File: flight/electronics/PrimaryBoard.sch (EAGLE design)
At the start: 10 parts

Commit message: primary board updates
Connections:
- net +5V: no longer ESP32.VIN
- net VBAT: now also ESP32.VIN
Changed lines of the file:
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@@
 <part name="ARDUCAM-B" library="Rembrandt Electronics - JST XH Connectors v1-0" deviceset="JST-XH-06-PIN" device=""/>
 <part name="GND8" library="supply1" library_urn="urn:adsk.eagle:library:371" deviceset="GND" device=""/>
-<part name="P+3" library="supply1" library_urn="urn:adsk.eagle:library:371" deviceset="+5V" device=""/>
 <part name="+3V4" library="supply1" library_urn="urn:adsk.eagle:library:371" deviceset="+3V3" device=""/>
 <part name="SENSOR_BOARD" library="Rembrandt Electronics - JST XH Connectors v1-0" deviceset="JST-XH-10-PIN" device=""/>
@@
 <attribute name="VALUE" x="22.86" y="-7.62" size="1.778" layer="96"/>
 </instance>
-<instance part="P+3" gate="1" x="50.8" y="88.9" smashed="yes">
-<attribute name="VALUE" x="48.26" y="83.82" size="1.778" layer="96" rot="R90"/>
-</instance>
 <instance part="+3V4" gate="G$1" x="22.86" y="17.78" smashed="yes">
 <attribute name="VALUE" x="20.32" y="12.7" size="1.778" layer="96" rot="R90"/>
@@
 <wire x1="114.3" y1="40.64" x2="116.84" y2="40.64" width="0.1524" layer="91"/>
 </segment>
-<segment>
-<pinref part="P+3" gate="1" pin="+5V"/>
-<wire x1="50.8" y1="86.36" x2="50.8" y2="83.82" width="0.1524" layer="91"/>
-<pinref part="ESP32" gate="G$1" pin="VIN"/>
-<wire x1="50.8" y1="83.82" x2="53.34" y2="83.82" width="0.1524" layer="91"/>
-</segment>
 </net>
 <net name="GND" class="0">
@@
 <wire x1="99.06" y1="111.76" x2="99.06" y2="71.12" width="0.1524" layer="91"/>
 <wire x1="99.06" y1="71.12" x2="106.68" y2="71.12" width="0.1524" layer="91"/>
+<pinref part="ESP32" gate="G$1" pin="VIN"/>
+<wire x1="50.8" y1="83.82" x2="53.34" y2="83.82" width="0.1524" layer="91"/>
+<wire x1="50.8" y1="83.82" x2="50.8" y2="111.76" width="0.1524" layer="91"/>
+<wire x1="50.8" y1="111.76" x2="99.06" y2="111.76" width="0.1524" layer="91"/>
+<junction x="99.06" y="111.76"/>
 </segment>
 </net>

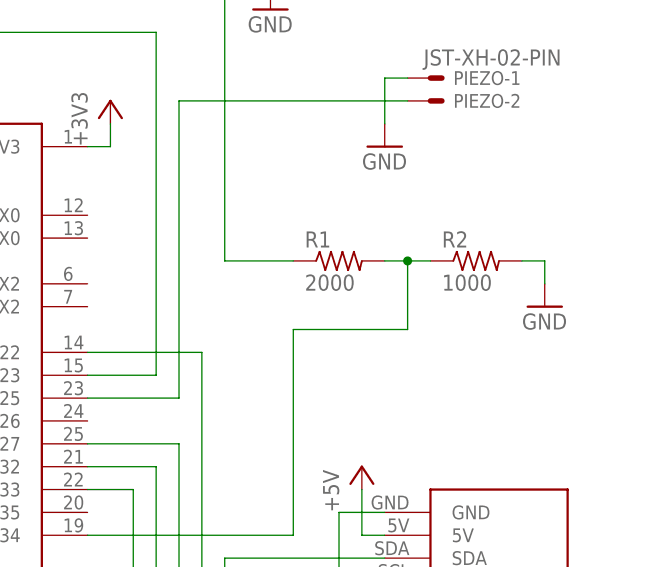
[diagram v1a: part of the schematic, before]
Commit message: shrink primary to 90mm
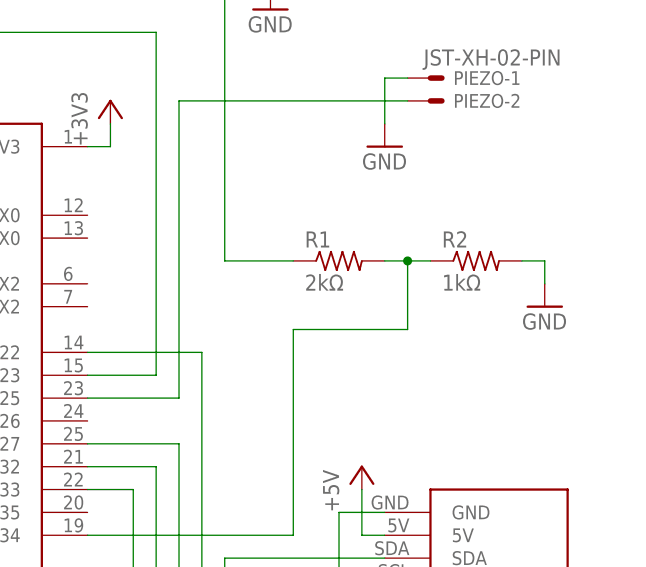
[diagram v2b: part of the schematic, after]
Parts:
- R1: value 2000 -> 2kΩ
- R2: value 1000 -> 1kΩ
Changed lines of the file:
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@@
 <part name="P+2" library="supply1" library_urn="urn:adsk.eagle:library:371" deviceset="+5V" device=""/>
 <part name="GND5" library="supply1" library_urn="urn:adsk.eagle:library:371" deviceset="GND" device=""/>
-<part name="R1" library="rcl" library_urn="urn:adsk.eagle:library:334" deviceset="R-US_" device="0207/10" package3d_urn="urn:adsk.eagle:package:23491/2" value="2000"/>
-<part name="R2" library="rcl" library_urn="urn:adsk.eagle:library:334" deviceset="R-US_" device="0207/10" package3d_urn="urn:adsk.eagle:package:23491/2" value="1000"/>
+<part name="R1" library="rcl" library_urn="urn:adsk.eagle:library:334" deviceset="R-US_" device="0207/10" package3d_urn="urn:adsk.eagle:package:23491/2" value="2kΩ"/>
+<part name="R2" library="rcl" library_urn="urn:adsk.eagle:library:334" deviceset="R-US_" device="0207/10" package3d_urn="urn:adsk.eagle:package:23491/2" value="1kΩ"/>
 <part name="GND6" library="supply1" library_urn="urn:adsk.eagle:library:371" deviceset="GND" device=""/>
 <part name="PIEZO" library="Rembrandt Electronics - JST XH Connectors v1-0" deviceset="JST-XH-02-PIN" device=""/>

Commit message: primary board redesign
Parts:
- removed SENSOR_BOARD: JST-XH-10-PIN, Rembrandt Electronics - JST XH Connectors v1-0:JST-XH-10-PIN
- added H1, H2, H3, H4: MOUNT-PAD-ROUND3.0, holes:MOUNT-PAD-ROUND3.0
- added X1: JST-XH-07-PIN, Rembrandt Electronics - JST XH Connectors v1-0:JST-XH-07-PIN
- U$2: value DS1307BREAKOUT -> PCF8523BREAKOUT; device Breakouts:DS1307BREAKOUT -> Breakouts:PCF8523BREAKOUT
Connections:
- removed net +5V: POWER_BOARD-3.S, U$2.5V
- removed net MOSI_CLK: ESP32.D14, SENSOR_BOARD-8.S, U$1.CLK
- new net HSPI_CLK: ESP32.D14, U$1.CLK
- net +3V3: now also POWER_BOARD-2.S, U$2.VCC, X1-2.S; no longer SENSOR_BOARD-10.S
- net GND: now also H1.MOUNT, H2.MOUNT, H3.MOUNT, H4.MOUNT, POWER_BOARD-1.S, X1-1.S; no longer POWER_BOARD-2.S, SENSOR_BOARD-9.S
- net GPIO1: now also X1-5.S; no longer SENSOR_BOARD-1.S
- net GPIO2: now also X1-6.S; no longer SENSOR_BOARD-2.S
- net GPIO3: now also X1-7.S; no longer SENSOR_BOARD-3.S
- net HSPI_MISO: no longer SENSOR_BOARD-7.S
- net HSPI_MOSI: no longer SENSOR_BOARD-6.S
- net I2C_SCL: now also X1-3.S; no longer SENSOR_BOARD-5.S
- net I2C_SDA: now also X1-4.S; no longer SENSOR_BOARD-4.S
- net SD_CS: now also ESP32.D15; no longer ESP32.D2
- net VBAT: now also POWER_BOARD-3.S; no longer ESP32.VIN, POWER_BOARD-1.S
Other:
- moved on the sheet: ARDUCAM-A-1, ARDUCAM-A-2, ARDUCAM-A-3, ARDUCAM-A-4, ARDUCAM-A-5, ARDUCAM-A-6, ARDUCAM-B-1, ARDUCAM-B-2, ARDUCAM-B-3, ARDUCAM-B-4, ARDUCAM-B-5, ARDUCAM-B-6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

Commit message: final board tweaks
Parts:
- removed POWER_BOARD: JST-XH-03-PIN, Rembrandt Electronics - JST XH Connectors v1-0:JST-XH-03-PIN
- added X2: JST-XH-03-PIN, JST-XH Connectors:JST-XH-03-PIN
- ARDUCAM-A, ARDUCAM-B: device Rembrandt Electronics - JST XH Connectors v1-0:JST-XH-06-PIN -> JST-XH Connectors:JST-XH-06-PIN
- PIEZO: device Rembrandt Electronics - JST XH Connectors v1-0:JST-XH-02-PIN -> JST-XH Connectors:JST-XH-02-PIN
- X1: device Rembrandt Electronics - JST XH Connectors v1-0:JST-XH-07-PIN -> JST-XH Connectors:JST-XH-07-PIN
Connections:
- net +3V3: now also X2-2.S; no longer POWER_BOARD-2.S
- net GND: now also X2-1.S; no longer POWER_BOARD-1.S
- net VBAT: now also X2-3.S; no longer POWER_BOARD-3.S
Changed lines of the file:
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@@
 <part name="GND1" library="supply1" library_urn="urn:adsk.eagle:library:371" deviceset="GND" device=""/>
 <part name="GND2" library="supply1" library_urn="urn:adsk.eagle:library:371" deviceset="GND" device=""/>
-<part name="ARDUCAM-A" library="Rembrandt Electronics - JST XH Connectors v1-0" deviceset="JST-XH-06-PIN" device="" value="JST-XH-06-PIN"/>
+<part name="ARDUCAM-A" library="JST-XH Connectors" deviceset="JST-XH-06-PIN" device="" value="JST-XH-06-PIN"/>
 <part name="GND3" library="supply1" library_urn="urn:adsk.eagle:library:371" deviceset="GND" device=""/>
 <part name="+3V3" library="supply1" library_urn="urn:adsk.eagle:library:371" deviceset="+3V3" device=""/>
 <part name="GND4" library="supply1" library_urn="urn:adsk.eagle:library:371" deviceset="GND" device=""/>
 <part name="U$1" library="Breakouts" deviceset="MICROSDBREAKOUT5V" device=""/>
-<part name="POWER_BOARD" library="Rembrandt Electronics - JST XH Connectors v1-0" deviceset="JST-XH-03-PIN" device=""/>
 <part name="GND5" library="supply1" library_urn="urn:adsk.eagle:library:371" deviceset="GND" device=""/>
 <part name="R1" library="rcl" library_urn="urn:adsk.eagle:library:334" deviceset="R-US_" device="0207/10" package3d_urn="urn:adsk.eagle:package:23491/2" value="2kΩ"/>
 <part name="R2" library="rcl" library_urn="urn:adsk.eagle:library:334" deviceset="R-US_" device="0207/10" package3d_urn="urn:adsk.eagle:package:23491/2" value="1kΩ"/>
 <part name="GND6" library="supply1" library_urn="urn:adsk.eagle:library:371" deviceset="GND" device=""/>
-<part name="PIEZO" library="Rembrandt Electronics - JST XH Connectors v1-0" deviceset="JST-XH-02-PIN" device=""/>
+<part name="PIEZO" library="JST-XH Connectors" deviceset="JST-XH-02-PIN" device=""/>
 <part name="GND7" library="supply1" library_urn="urn:adsk.eagle:library:371" deviceset="GND" device=""/>
-<part name="ARDUCAM-B" library="Rembrandt Electronics - JST XH Connectors v1-0" deviceset="JST-XH-06-PIN" device=""/>
+<part name="ARDUCAM-B" library="JST-XH Connectors" deviceset="JST-XH-06-PIN" device=""/>
 <part name="GND8" library="supply1" library_urn="urn:adsk.eagle:library:371" deviceset="GND" device=""/>
 <part name="+3V4" library="supply1" library_urn="urn:adsk.eagle:library:371" deviceset="+3V3" device=""/>
 <part name="+3V5" library="supply1" library_urn="urn:adsk.eagle:library:371" deviceset="+3V3" device=""/>
 <part name="GND9" library="supply1" library_urn="urn:adsk.eagle:library:371" deviceset="GND" device=""/>
-<part name="X1" library="Rembrandt Electronics - JST XH Connectors v1-0" deviceset="JST-XH-07-PIN" device=""/>
+<part name="X1" library="JST-XH Connectors" deviceset="JST-XH-07-PIN" device=""/>
 <part name="+3V6" library="supply1" library_urn="urn:adsk.eagle:library:371" deviceset="+3V3" device=""/>
 <part name="U$2" library="Breakouts" deviceset="PCF8523BREAKOUT" device=""/>
@@
 <part name="H4" library="holes" library_urn="urn:adsk.eagle:library:237" deviceset="MOUNT-PAD-ROUND" device="3.0" package3d_urn="urn:adsk.eagle:package:14280/1"/>
 <part name="GND10" library="supply1" library_urn="urn:adsk.eagle:library:371" deviceset="GND" device=""/>
+<part name="X2" library="JST-XH Connectors" deviceset="JST-XH-03-PIN" device=""/>
 </parts>
 <sheets>
@@
 </instance>
 <instance part="U$1" gate="G$1" x="-27.94" y="60.96" smashed="yes" rot="MR0"/>
-<instance part="POWER_BOARD" gate="-1" x="109.22" y="111.76" smashed="yes">
-<attribute name="NAME" x="111.76" y="110.998" size="1.524" layer="95"/>
-<attribute name="VALUE" x="108.458" y="113.157" size="1.778" layer="96"/>
-</instance>
-<instance part="POWER_BOARD" gate="-2" x="109.22" y="109.22" smashed="yes">
-<attribute name="NAME" x="111.76" y="108.458" size="1.524" layer="95"/>
-</instance>
-<instance part="POWER_BOARD" gate="-3" x="109.22" y="106.68" smashed="yes">
-<attribute name="NAME" x="111.76" y="105.918" size="1.524" layer="95"/>
-</instance>
 <instance part="GND5" gate="1" x="111.76" y="27.94" smashed="yes">
 <attribute name="VALUE" x="109.22" y="25.4" size="1.778" layer="96"/>
@@
 <instance part="GND10" gate="1" x="53.34" y="-55.88" smashed="yes">
 <attribute name="VALUE" x="50.8" y="-58.42" size="1.778" layer="96"/>
+</instance>
+<instance part="X2" gate="-1" x="109.22" y="111.76" smashed="yes">
+<attribute name="NAME" x="111.76" y="110.998" size="1.524" layer="95"/>
+<attribute name="VALUE" x="108.458" y="113.157" size="1.778" layer="96"/>
+</instance>
+<instance part="X2" gate="-2" x="109.22" y="109.22" smashed="yes">
+<attribute name="NAME" x="111.76" y="108.458" size="1.524" layer="95"/>
+</instance>
+<instance part="X2" gate="-3" x="109.22" y="106.68" smashed="yes">
+<attribute name="NAME" x="111.76" y="105.918" size="1.524" layer="95"/>
 </instance>
 </instances>
@@
 <segment>
 <pinref part="GND4" gate="1" pin="GND"/>
-<wire x1="104.14" y1="109.22" x2="104.14" y2="104.14" width="0.1524" layer="91"/>
-<pinref part="POWER_BOARD" gate="-1" pin="S"/>
-<wire x1="104.14" y1="104.14" x2="104.14" y2="101.6" width="0.1524" layer="91"/>
+<wire x1="104.14" y1="111.76" x2="104.14" y2="101.6" width="0.1524" layer="91"/>
+<pinref part="X2" gate="-1" pin="S"/>
 <wire x1="106.68" y1="111.76" x2="104.14" y2="111.76" width="0.1524" layer="91"/>
-<wire x1="104.14" y1="111.76" x2="104.14" y2="109.22" width="0.1524" layer="91"/>
 </segment>
 <segment>
@@
 <segment>
 <pinref part="+3V6" gate="G$1" pin="+3V3"/>
-<pinref part="POWER_BOARD" gate="-2" pin="S"/>
 <wire x1="101.6" y1="109.22" x2="101.6" y2="116.84" width="0.1524" layer="91"/>
-<wire x1="106.68" y1="109.22" x2="101.6" y2="109.22" width="0.1524" layer="91"/>
+<pinref part="X2" gate="-2" pin="S"/>
+<wire x1="101.6" y1="109.22" x2="106.68" y2="109.22" width="0.1524" layer="91"/>
 </segment>
 <segment>
@@
 <net name="VBAT" class="0">
 <segment>
-<label x="99.06" y="106.68" size="1.778" layer="95" rot="MR0" xref="yes"/>
-<pinref part="POWER_BOARD" gate="-3" pin="S"/>
-<wire x1="106.68" y1="106.68" x2="99.06" y2="106.68" width="0.1524" layer="91"/>
-</segment>
-<segment>
 <pinref part="R1" gate="G$1" pin="1"/>
 <wire x1="134.62" y1="73.66" x2="137.16" y2="73.66" width="0.1524" layer="91"/>
 <label x="134.62" y="73.66" size="1.778" layer="95" rot="MR0" xref="yes"/>
 </segment>
-</net>
+<segment>
+<pinref part="X2" gate="-3" pin="S"/>
+<wire x1="106.68" y1="106.68" x2="99.06" y2="106.68" width="0.1524" layer="91"/>
+<label x="99.06" y="106.68" size="1.778" layer="95" rot="MR0" xref="yes"/>
+</segment>
+</net>
